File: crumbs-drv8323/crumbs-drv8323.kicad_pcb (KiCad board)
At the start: 2 copper layers, 1 part, among them U1 DRV8323SRTAT

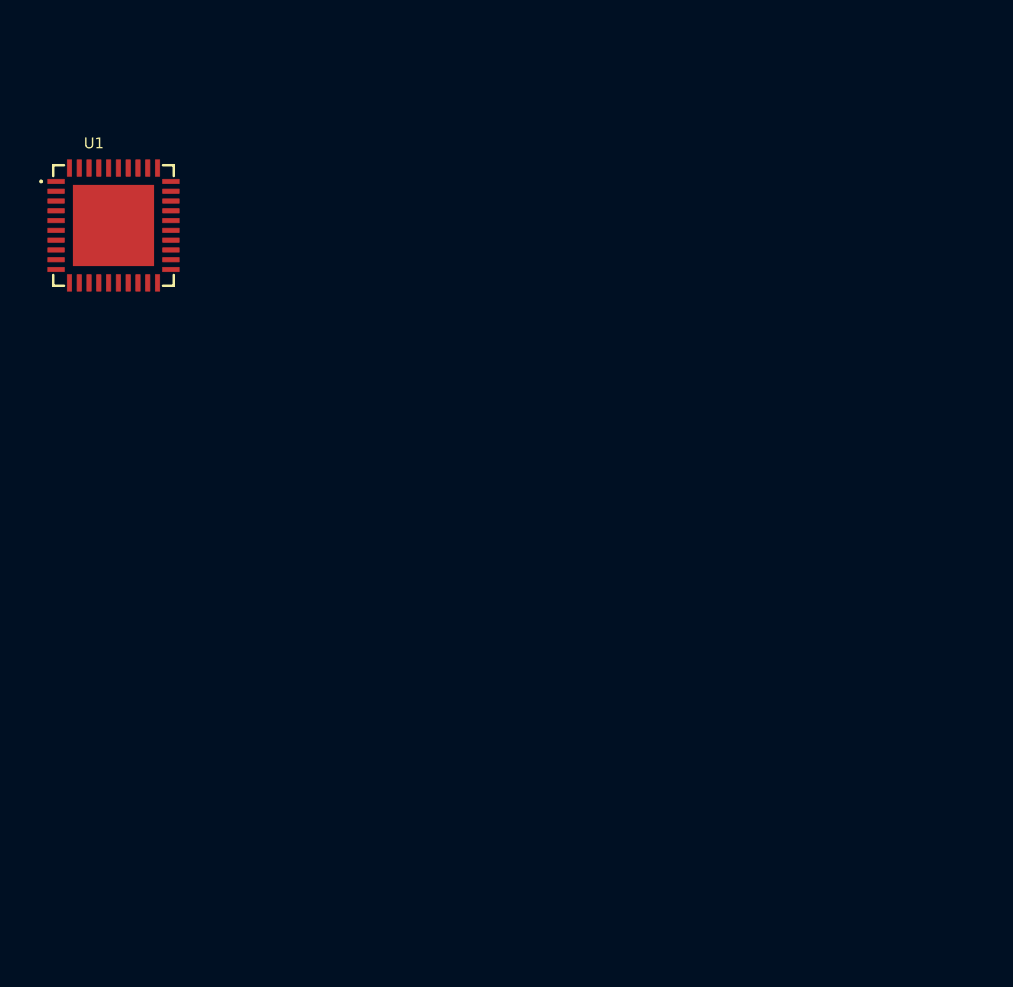
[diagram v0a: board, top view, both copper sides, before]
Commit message: feat: first iteration on drv8323 schematic
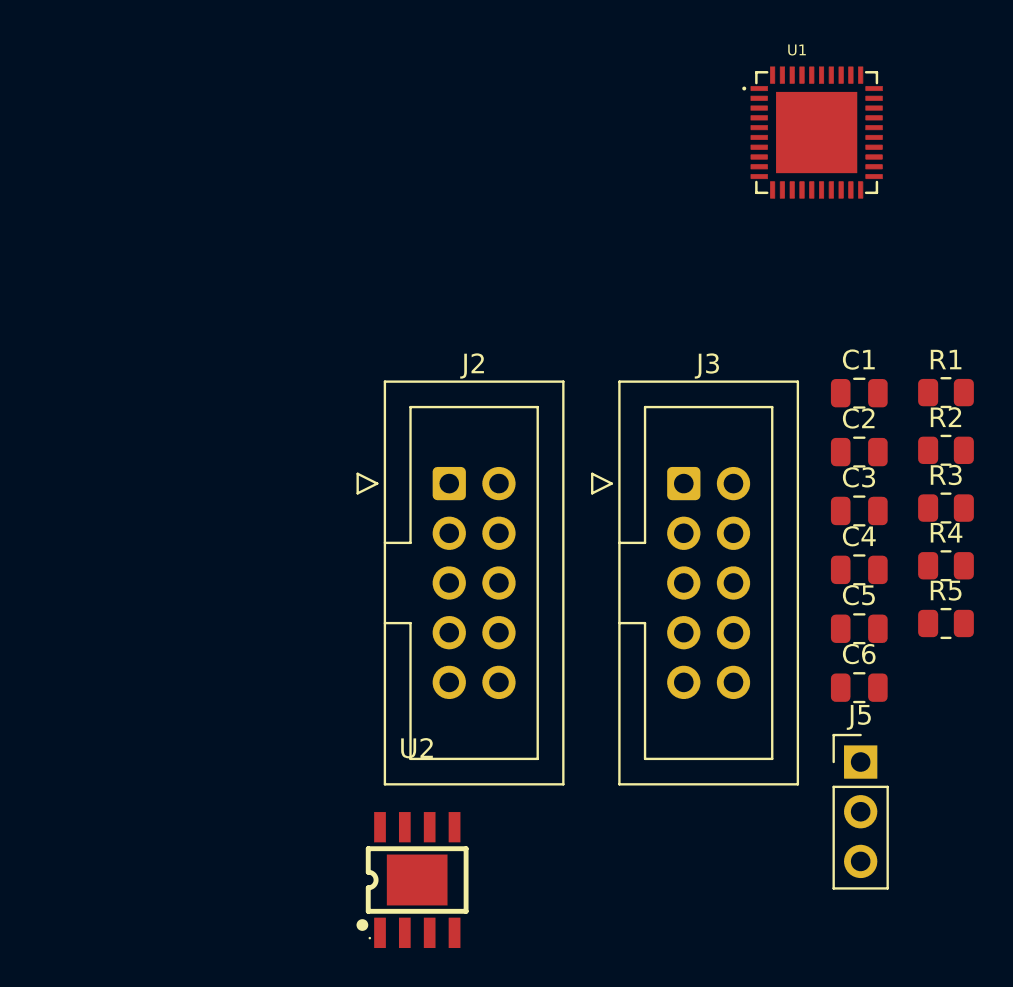
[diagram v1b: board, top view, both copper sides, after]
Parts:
- added C1: 1uF, Capacitor_SMD:C_0805_2012Metric, F.Cu at (90.4, 49.6)
- added C2: 100nF, Capacitor_SMD:C_0805_2012Metric, F.Cu at (90.4, 52.6)
- added C3: 22uF, Capacitor_SMD:C_0805_2012Metric, F.Cu at (90.4, 55.6)
- added C4: 47nF, Capacitor_SMD:C_0805_2012Metric, F.Cu at (90.4, 58.6)
- added C5: 100nF, Capacitor_SMD:C_0805_2012Metric, F.Cu at (90.4, 61.6)
- added C6: 1uF/6.3V, Capacitor_SMD:C_0805_2012Metric, F.Cu at (90.4, 64.6)
- added J2: Conn_02x05_Odd_Even, Connector_IDC:IDC-Header_2x05_P2.54mm_Vertical, F.Cu at (69.5, 54.2)
- added J3: Conn_02x05_Odd_Even, Connector_IDC:IDC-Header_2x05_P2.54mm_Vertical, F.Cu at (81.5, 54.2)
- added J5: Conn_01x03, Connector_PinHeader_2.54mm:PinHeader_1x03_P2.54mm_Vertical, F.Cu at (90.5, 68.4)
- added R1: RSense, Resistor_SMD:R_0805_2012Metric, F.Cu at (94.9, 49.5)
- added R2: RSense, Resistor_SMD:R_0805_2012Metric, F.Cu at (94.9, 52.5)
- added R3: RSense, Resistor_SMD:R_0805_2012Metric, F.Cu at (94.9, 55.4)
- added R4: 4K7, Resistor_SMD:R_0805_2012Metric, F.Cu at (94.9, 58.4)
- added R5: 4K7, Resistor_SMD:R_0805_2012Metric, F.Cu at (94.9, 61.3)
- added U2: LMR16010PDDAR, easyeda2kicad:SOPOWERPAD-8_L4.9-W3.9-P1.27-LS6.0-BL-EP, F.Cu at (67.8, 74.5)
- moved U1 36.2 mm to (88.2, 36.2)
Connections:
- U1 pad 1: unconnected-(U1-CPL-Pad1) -> Net-(U1-CPL)
- U1 pad 10: unconnected-(U1-SNA-Pad10) -> GND
- U1 pad 11: unconnected-(U1-SNB-Pad11) -> GND
- U1 pad 12: unconnected-(U1-SPB-Pad12) -> Net-(U1-SPB)
- U1 pad 13: unconnected-(U1-GLB-Pad13) -> Net-(U1-GLB)
- U1 pad 14: unconnected-(U1-SHB-Pad14) -> Net-(J1-Pin_2)
- U1 pad 15: unconnected-(U1-GHB-Pad15) -> Net-(U1-GHB)
- U1 pad 16: unconnected-(U1-GHC-Pad16) -> Net-(U1-GHC)
- U1 pad 17: unconnected-(U1-SHC-Pad17) -> Net-(J1-Pin_3)
- U1 pad 18: unconnected-(U1-GLC-Pad18) -> Net-(U1-GLC)
- U1 pad 19: unconnected-(U1-SPC-Pad19) -> Net-(U1-SPC)
- U1 pad 2: unconnected-(U1-CPH-Pad2) -> Net-(U1-CPH)
- U1 pad 20: unconnected-(U1-SNC-Pad20) -> GND
- U1 pad 21: unconnected-(U1-SOC-Pad21) -> /SOC
- U1 pad 22: unconnected-(U1-SOB-Pad22) -> /SOB
- U1 pad 23: unconnected-(U1-SOA-Pad23) -> /SOA
- U1 pad 24: unconnected-(U1-VREF-Pad24) -> VCC
- U1 pad 25: unconnected-(U1-NFAULT-Pad25) -> /NFAULT
- U1 pad 26: unconnected-(U1-SDO-Pad26) -> /SDO
- U1 pad 27: unconnected-(U1-SDI-Pad27) -> /SDI
- U1 pad 28: unconnected-(U1-SCLK-Pad28) -> /SCLK
- U1 pad 29: unconnected-(U1-NSCS-Pad29) -> /NSCS
- U1 pad 3: unconnected-(U1-VCP-Pad3) -> Net-(U1-VCP)
- U1 pad 30: unconnected-(U1-ENABLE-Pad30) -> /ENABLE
- U1 pad 31: unconnected-(U1-CAL-Pad31) -> /CAL
- U1 pad 32: unconnected-(U1-AGND-Pad32) -> GND
- U1 pad 33: unconnected-(U1-DVDD-Pad33) -> DVDD
- U1 pad 34: unconnected-(U1-INHA-Pad34) -> /INHA
- U1 pad 35: unconnected-(U1-INLA-Pad35) -> /INLA
- U1 pad 36: unconnected-(U1-INHB-Pad36) -> /INHB
- U1 pad 37: unconnected-(U1-INLB-Pad37) -> /INLB
- U1 pad 38: unconnected-(U1-INHC-Pad38) -> /INHC
- U1 pad 39: unconnected-(U1-INLC-Pad39) -> /INLC
- U1 pad 4: unconnected-(U1-VM-Pad4) -> VM
- U1 pad 40: unconnected-(U1-PGND-Pad40) -> GND
- U1 pad 5: unconnected-(U1-VDRAIN-Pad5) -> VM
- U1 pad 6: unconnected-(U1-GHA-Pad6) -> Net-(U1-GHA)
- U1 pad 7: unconnected-(U1-SHA-Pad7) -> Net-(J1-Pin_1)
- U1 pad 8: unconnected-(U1-GLA-Pad8) -> Net-(U1-GLA)
- U1 pad 9: unconnected-(U1-SPA-Pad9) -> Net-(U1-SPA)

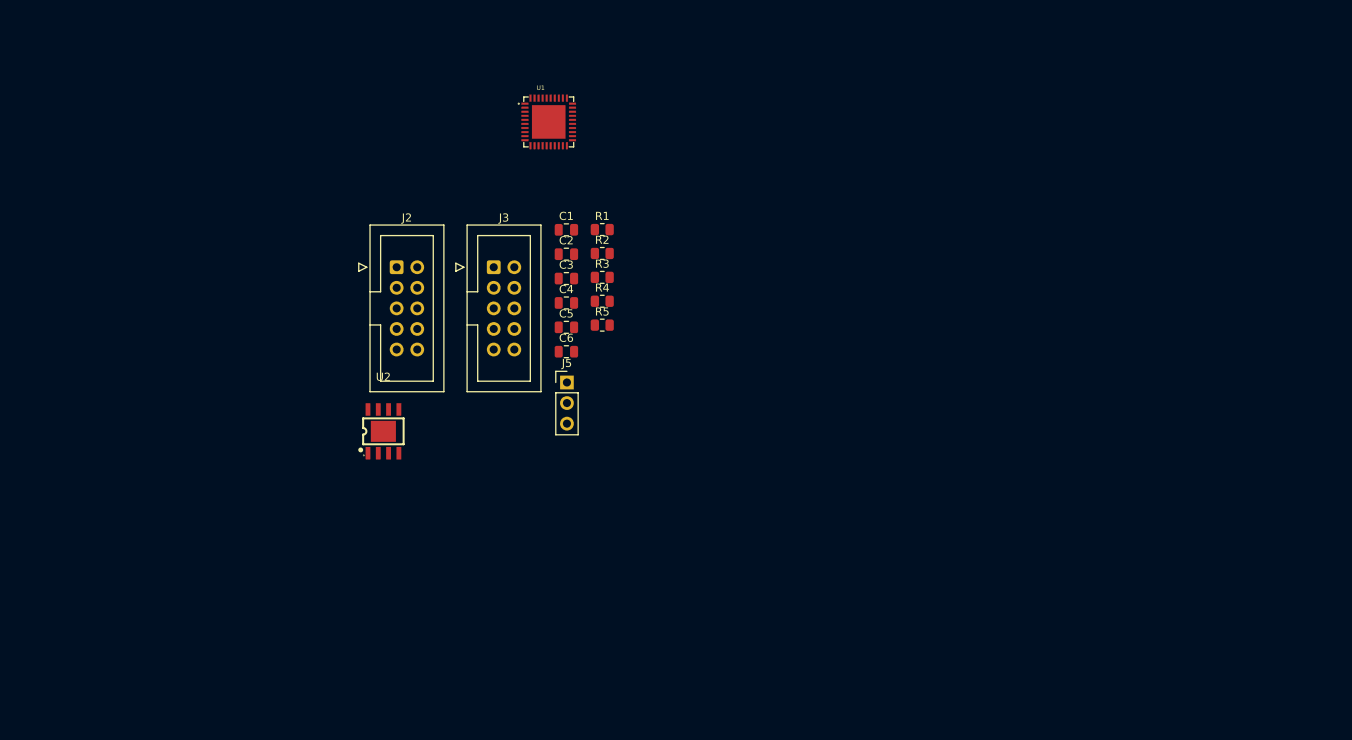
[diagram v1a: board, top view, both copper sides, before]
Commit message: feat: assign correct footprint
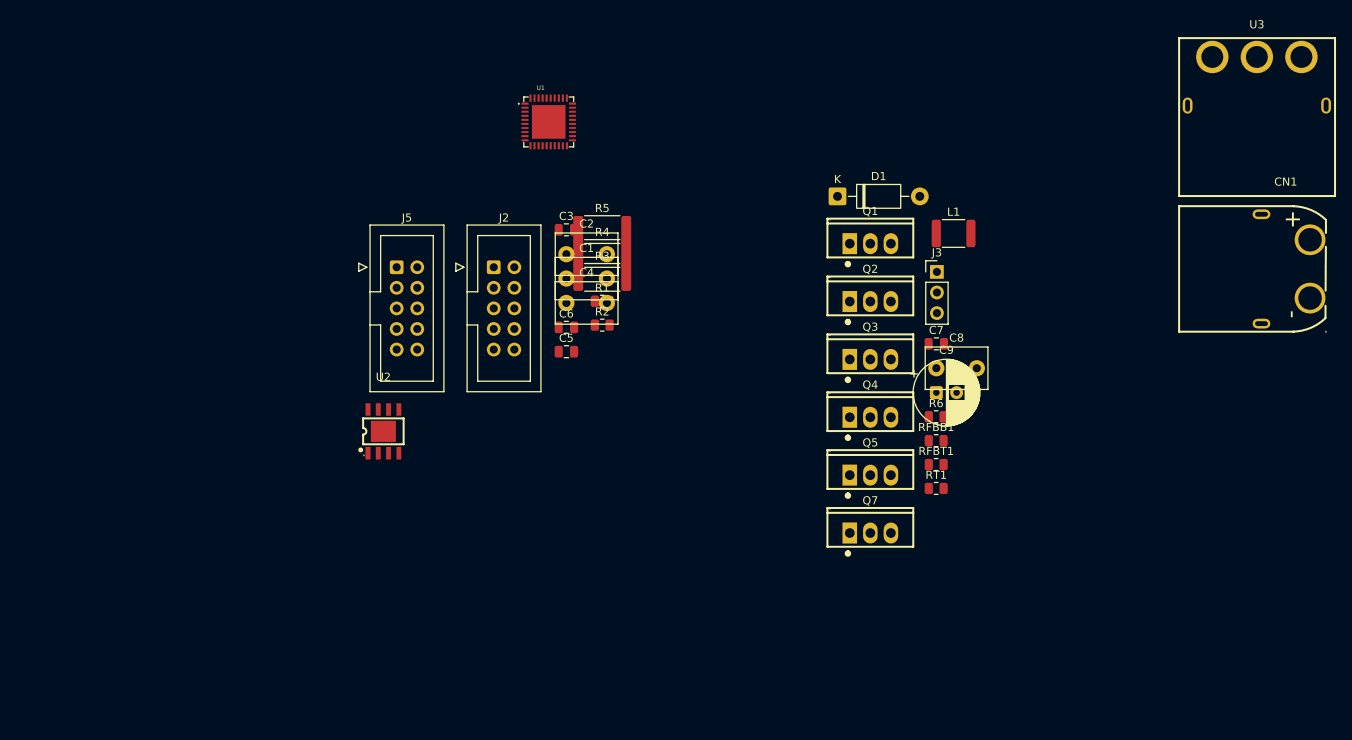
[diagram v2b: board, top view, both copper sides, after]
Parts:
- removed the J5 at (90.5, 68.4)
- added C7: 100nF / 16V, Capacitor_SMD:C_0805_2012Metric, F.Cu at (136.1, 63.6)
- added C8: 47uF / 16V, Capacitor_THT:C_Disc_D7.5mm_W5.0mm_P5.00mm, F.Cu at (136.1, 66.7)
- added C9: 4.7uF / VM, Capacitor_THT:CP_Radial_D8.0mm_P2.50mm, F.Cu at (136.1, 69.7)
- added CN1: XT60PW-M, easyeda2kicad:CONN-TH_XT60PW-M, F.Cu at (179.2, 54.4)
- added D1: 1N5819, Diode_THT:D_DO-41_SOD81_P10.16mm_Horizontal, F.Cu at (123.9, 45.4)
- added J3: VCC_to_3.3V, Connector_PinHeader_2.54mm:PinHeader_1x03_P2.54mm_Vertical, F.Cu at (136.2, 54.8)
- added L1: 22uH / 2A, Inductor_SMD:L_1812_4532Metric, F.Cu at (138.2, 50.0)
- added Q1: IRFB3077PBF, easyeda2kicad:TO-220-3_L10.0-W4.5-P2.54-L, F.Cu at (128.0, 51.3)
- added Q2: IRFB3077PBF, easyeda2kicad:TO-220-3_L10.0-W4.5-P2.54-L, F.Cu at (128.0, 58.4)
- added Q3: IRFB3077PBF, easyeda2kicad:TO-220-3_L10.0-W4.5-P2.54-L, F.Cu at (128.0, 65.6)
- added Q4: IRFB3077PBF, easyeda2kicad:TO-220-3_L10.0-W4.5-P2.54-L, F.Cu at (128.0, 72.7)
- added Q5: IRFB3077PBF, easyeda2kicad:TO-220-3_L10.0-W4.5-P2.54-L, F.Cu at (128.0, 79.9)
- added Q7: IRFB3077PBF, easyeda2kicad:TO-220-3_L10.0-W4.5-P2.54-L, F.Cu at (128.0, 87.0)
- added R6: 4K7, Resistor_SMD:R_0805_2012Metric, F.Cu at (136.1, 72.7)
- added RFBB1: 30K, Resistor_SMD:R_0805_2012Metric, F.Cu at (136.1, 75.6)
- added RFBT1: 100K, Resistor_SMD:R_0805_2012Metric, F.Cu at (136.1, 78.5)
- added RT1: 34K8, Resistor_SMD:R_0805_2012Metric, F.Cu at (136.1, 81.5)
- added U3: MR60PW-M.G.B, easyeda2kicad:CONN-TH_MR60PW, F.Cu at (175.7, 31.2)
- C1: renamed from C3; footprint Capacitor_SMD:C_0805_2012Metric -> Capacitor_THT:C_Disc_D7.5mm_W5.0mm_P5.00mm
- C2, C4: footprint Capacitor_SMD:C_0805_2012Metric -> Capacitor_THT:C_Disc_D7.5mm_W5.0mm_P5.00mm
- C3: renamed from C1; value 1uF -> 1uF/16V
- R3: value RSense -> 2m / 2W; footprint Resistor_SMD:R_0805_2012Metric -> Resistor_SMD:R_2512_6332Metric
- R4: renamed from R2; value RSense -> 2m / 2W; footprint Resistor_SMD:R_0805_2012Metric -> Resistor_SMD:R_2512_6332Metric
- R5: renamed from R1; value RSense -> 2m / 2W; footprint Resistor_SMD:R_0805_2012Metric -> Resistor_SMD:R_2512_6332Metric
- renumbered C6 to C5, C5 to C6, J3 to J2, J2 to J5, R4 to R1, R5 to R2
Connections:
- J5 pad 10: unconnected-(J2-Pin_10-Pad10) -> GND
- J5 pad 6: unconnected-(J2-Pin_6-Pad6) -> VM
- J5 pad 8: GND -> +3V3
- U1 pad 41: unconnected-(U1-EXP-Pad41) -> GND
- U2 pad 1: unconnected-(U2-BOOT-Pad1) -> Net-(U2-BOOT)
- U2 pad 2: unconnected-(U2-VIN-Pad2) -> VM
- U2 pad 3: unconnected-(U2-EN-Pad3) -> VM
- U2 pad 4: unconnected-(U2-RT/SYNC-Pad4) -> Net-(U2-RT/SYNC)
- U2 pad 5: unconnected-(U2-FB-Pad5) -> Net-(U2-FB)
- U2 pad 6: unconnected-(U2-PGOOD-Pad6) -> /PGOOD
- U2 pad 7: unconnected-(U2-GND-Pad7) -> GND
- U2 pad 8: unconnected-(U2-SW-Pad8) -> Net-(D1-K)
- U2 pad 9: unconnected-(U2-EP-Pad9) -> GND

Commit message: feat: drv8323 finish routing
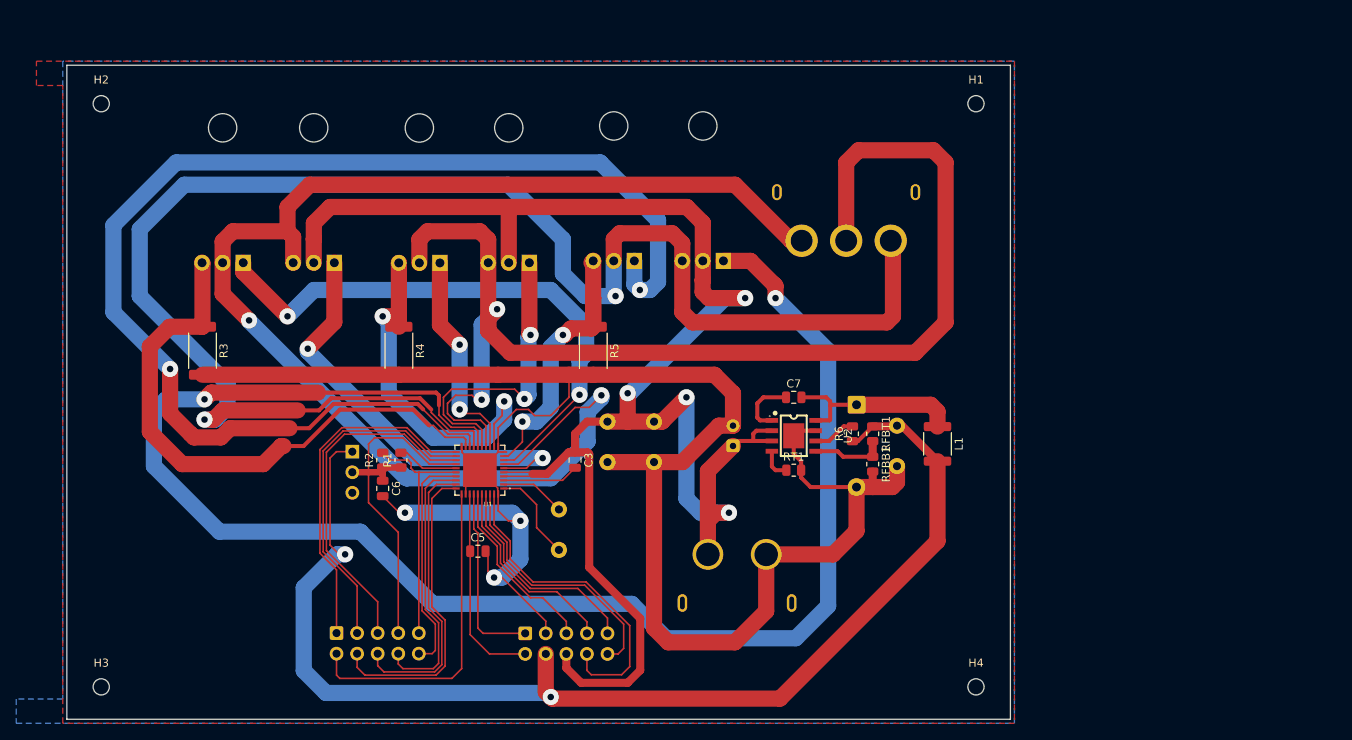
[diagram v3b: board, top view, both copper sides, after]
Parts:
- added H1: MountingHole, MountingHole:MountingHole_2mm, F.Cu at (141.0, 34.0)
- added H2: MountingHole, MountingHole:MountingHole_2mm, F.Cu at (33.0, 34.0)
- added H3: MountingHole, MountingHole:MountingHole_2mm, F.Cu at (33.0, 106.0)
- added H4: MountingHole, MountingHole:MountingHole_2mm, F.Cu at (141.0, 106.0)
- C1, C2, C4, C8, C9, CN1, D1, J2, J3, J5, U3: moved to B.Cu
- Q1, Q2, Q3, Q4, Q5, Q7: footprint easyeda2kicad:TO-220-3_L10.0-W4.5-P2.54-L -> Package_TO_SOT_THT:TO-220-3_Horizontal_TabDown; moved to B.Cu
- moved CN1 77.8 mm to (111.5, 92.6), turned to 90 degrees
- moved Q1 77.5 mm to (50.5, 53.6), turned to 180 degrees
- moved J3 75.5 mm to (64.0, 77.0), turned to 180 degrees
- moved Q7 74.1 mm to (61.8, 53.6), turned to 180 degrees
- moved Q3 54.5 mm to (74.8, 53.7), turned to 180 degrees
- moved U3 53.4 mm to (125.0, 47.9)
- moved U2 50.7 mm to (118.5, 75.0), turned to -90 degrees
- moved R3 50.2 mm to (45.5, 64.5), turned to -90 degrees
- moved J2 49.2 mm to (62.1, 99.4), turned to -90 degrees
- moved J5 47.9 mm to (85.3, 99.4), turned to -90 degrees
- moved U1 43.8 mm to (79.8, 79.2), turned to 180 degrees
- moved Q2 42.4 mm to (85.9, 53.6), turned to 180 degrees
- moved Q5 39.4 mm to (98.8, 53.4), turned to 180 degrees
- moved R2 31.8 mm to (67.8, 78.0), turned to 90 degrees
- moved R1 31.7 mm to (70.0, 78.0), turned to 90 degrees
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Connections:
- net Net-(Q1-D) renamed /sha
- net Net-(Q1-G) renamed /gla
- net Net-(Q1-S) renamed /spc
- net Net-(Q2-G) renamed /ghb
- net Net-(Q2-S) renamed /shb
- net Net-(Q3-G) renamed /glb
- net Net-(Q3-S) renamed /spb
- net Net-(Q4-G) renamed /ghc
- net Net-(Q4-S) renamed /shc
- net Net-(Q5-G) renamed /glc
- net Net-(Q5-S) renamed /spa
- net Net-(Q7-G) renamed /gha
- net Net-(U1-CPH) renamed /cph
- net Net-(U1-CPL) renamed /cpl
- J2 pad 1: /SDI -> /SOC
- J2 pad 10: /INLB -> /SDI
- J2 pad 2: /ENABLE -> /CAL
- J2 pad 3: /SDO -> /SOB
- J2 pad 4: /INHA -> /ENABLE
- J2 pad 5: /SCLK -> /SOA
- J2 pad 6: /INLA -> /NSCS
- J2 pad 7: /INHC -> VCC
- J2 pad 8: /INHB -> /SCLK
- J2 pad 9: /INLC -> /SDO
- J5 pad 1: /NSCS -> /INHA
- J5 pad 10: GND -> /INHC
- J5 pad 3: /SOC -> GND
- J5 pad 4: VCC -> +3V3
- J5 pad 5: /SOB -> /INLA
- J5 pad 7: /SOA -> /INHB
- J5 pad 8: +3V3 -> /INLC
- J5 pad 9: /CAL -> /INLB
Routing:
- net GND: track 0.00 -> 252.5 mm, vias 0 -> 3
- net VM: track 0.00 -> 218.3 mm, vias 0 -> 4
- net /shc: track 0.00 -> 198.4 mm, vias 0 -> 2
- net /ghc: track 0.00 -> 196.6 mm, vias 0 -> 2
- net /sha: track 0.00 -> 168.1 mm, vias 0 -> 2
- net /glc: track 0.00 -> 162.9 mm, vias 0 -> 2
- net /shb: track 0.00 -> 154.7 mm, vias 0 -> 2
- net +3V3: track 0.00 -> 149.5 mm, vias 0 -> 2
- net /spc: track 0.00 -> 71.8 mm
- net /gla: track 0.00 -> 70.5 mm, vias 0 -> 2
- net /gha: track 0.00 -> 52.1 mm, vias 0 -> 2
- net /spb: track 0.00 -> 45.5 mm, vias 0 -> 2
- net VCC: track 0.00 -> 45.0 mm
- net /SOA: track 0.00 -> 43.2 mm
- net /SOB: track 0.00 -> 42.9 mm
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- added copper zone on B.Cu, net (none)
- added copper zone on F.Cu, net (none)
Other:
- board outline added: 116.5 x 80.8 mm
